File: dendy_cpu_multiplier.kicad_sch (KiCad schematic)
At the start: 12 parts, among them J1 CLK_IN, J2 CPU Connections, U1 74ACT74, U2 ICS501

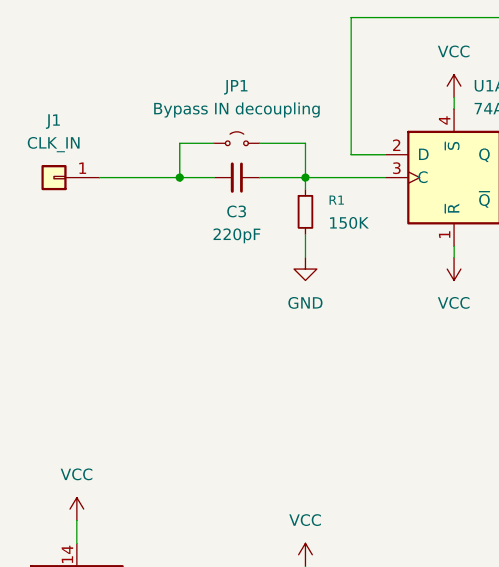
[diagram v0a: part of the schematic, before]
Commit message: Move around the components to fit into the holes of a DIP40 socket
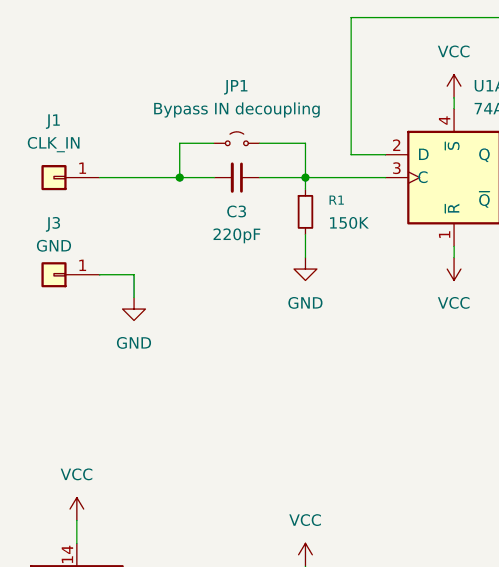
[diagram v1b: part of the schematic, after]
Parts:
- added J3: GND, TestPoint:TestPoint_Pad_D1.5mm, symbol Connector_Generic:Conn_01x01
- J1: footprint TestPoint:TestPoint_Pad_D3.0mm -> TestPoint:TestPoint_Pad_D1.5mm
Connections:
- net GND: now also J3.1 (Pin_1)
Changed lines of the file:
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@@
+	(wire
+		(pts
+			(xy 54.61 55.245) (xy 54.61 57.785)
+		)
+		(stroke
+			(width 0)
+			(type default)
+		)
+	)
 	(wire
 		(pts
@@
 		(pts
 			(xy 105.41 46.99) (xy 105.41 44.45)
+		)
+		(stroke
+			(width 0)
+			(type default)
+		)
+	)
+	(wire
+		(pts
+			(xy 50.8 55.245) (xy 54.61 55.245)
 		)
 		(stroke
@@
 	)
 	(symbol
+		(lib_id "Connector_Generic:Conn_01x01")
+		(at 45.72 55.245 180)
+		(unit 1)
+		(exclude_from_sim no)
+		(in_bom yes)
+		(on_board yes)
+		(dnp no)
+		(fields_autoplaced yes)
+		(property "Reference" "J3"
+			(at 45.72 49.53 0)
+			(effects
+				(font
+					(size 1.27 1.27)
+				)
+			)
+		)
+		(property "Value" "GND"
+			(at 45.72 52.07 0)
+			(effects
+				(font
+					(size 1.27 1.27)
+				)
+			)
+		)
+		(property "Footprint" "TestPoint:TestPoint_Pad_D1.5mm"
+			(at 45.72 55.245 0)
+			(effects
+				(font
+					(size 1.27 1.27)
+				)
+				(hide yes)
+			)
+		)
+		(property "Datasheet" "~"
+			(at 45.72 55.245 0)
+			(effects
+				(font
+					(size 1.27 1.27)
+				)
+				(hide yes)
+			)
+		)
+		(property "Description" "Generic connector, single row, 01x01, script generated (kicad-library-utils/schlib/autogen/connector/)"
+			(at 45.72 55.245 0)
+			(effects
+				(font
+					(size 1.27 1.27)
+				)
+				(hide yes)
+			)
+		)
+		(pin "1"
+		)
+		(instances
+			(project "dendy_cpu_multiplier"
+				(path "/e570d65d-aa38-4930-a27b-b21b582b3289"
+					(reference "J3")
+					(unit 1)
+				)
+			)
+		)
+	)
+	(symbol
 		(lib_id "power:VCC")
 		(at 120.65 53.34 180)
@@
 			)
 		)
-		(property "Footprint" "TestPoint:TestPoint_Pad_D3.0mm"
+		(property "Footprint" "TestPoint:TestPoint_Pad_D1.5mm"
 			(at 45.72 44.45 0)
 			(effects
@@
 					(unit 1)
 				)
+			)
+		)
+	)
+	(symbol
+		(lib_id "power:GND")
+		(at 54.61 57.785 0)
+		(unit 1)
+		(exclude_from_sim no)
+		(in_bom yes)
+		(on_board yes)
+		(dnp no)
+		(fields_autoplaced yes)
+		(property "Reference" "#PWR017"
+			(at 54.61 64.135 0)
+			(effects
+				(font
+					(size 1.27 1.27)
+				)
+				(hide yes)
+			)
+		)
+		(property "Value" "GND"
+			(at 54.61 62.865 0)
+			(effects
+				(font
+					(size 1.27 1.27)
+				)
+			)
+		)
+		(property "Footprint" ""
+			(at 54.61 57.785 0)
+			(effects
+				(font
+					(size 1.27 1.27)
+				)
+				(hide yes)
+			)
+		)
+		(property "Datasheet" ""
+			(at 54.61 57.785 0)
+			(effects
+				(font
+					(size 1.27 1.27)
+				)
+				(hide yes)
+			)
+		)
+		(property "Description" "Power symbol creates a global label with name \"GND\" , ground"
+			(at 54.61 57.785 0)
+			(effects
+				(font
+					(size 1.27 1.27)
+				)
+				(hide yes)
+			)
+		)
+		(pin "1"
+		)
+		(instances
+			(project "dendy_cpu_multiplier"
+				(path "/e570d65d-aa38-4930-a27b-b21b582b3289"
+					(reference "#PWR017")
+					(unit 1)
+				)
